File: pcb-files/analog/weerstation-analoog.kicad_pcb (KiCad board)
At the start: 2 copper layers, 99.1 x 99.1 mm, 60 parts, among them J1 i2c in out, J10 regensensor2 pins, J11 adc_alerts, J12 sound meter, J13 ADC 4 inputs, J2 power-in, J3 ads1115 (1), J4 ads1115 (2), J5 ads1115 (4), J6 ads1115 (3)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

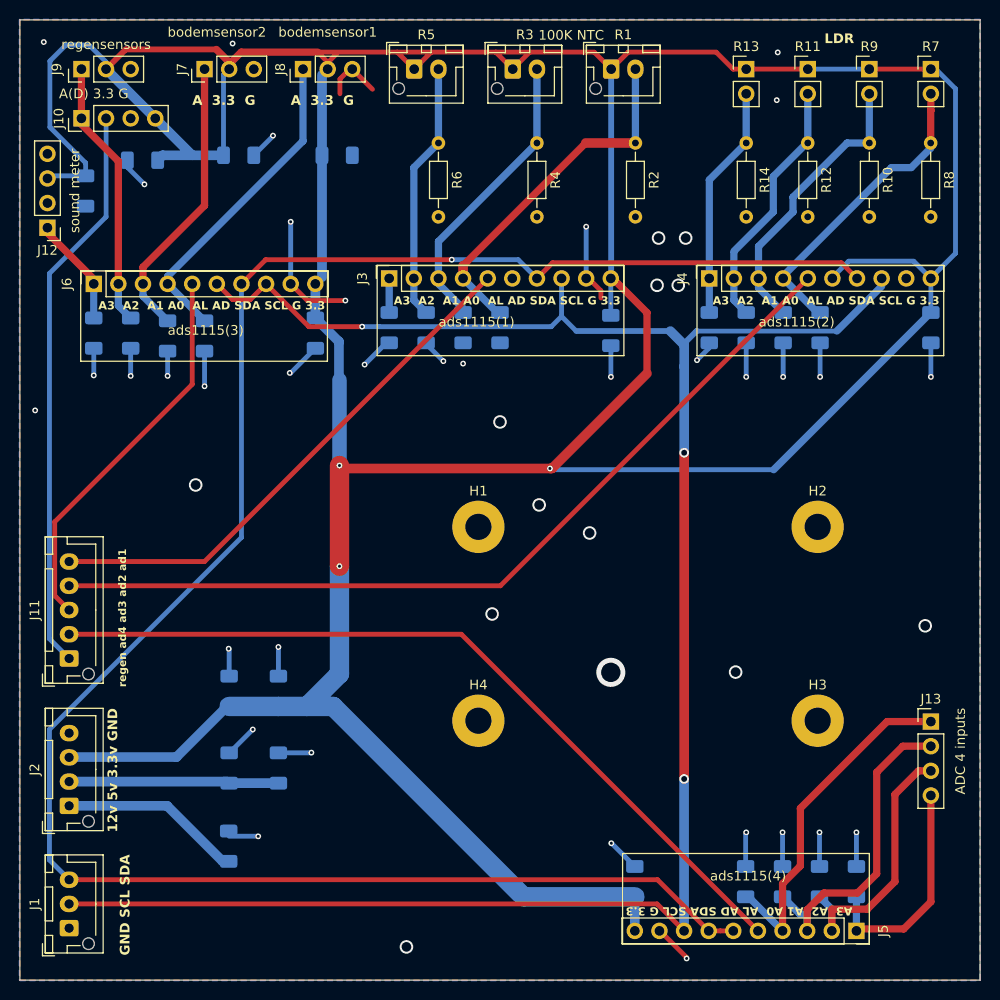
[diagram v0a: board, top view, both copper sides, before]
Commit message: pcbs as orderd. loads of grounding fixes
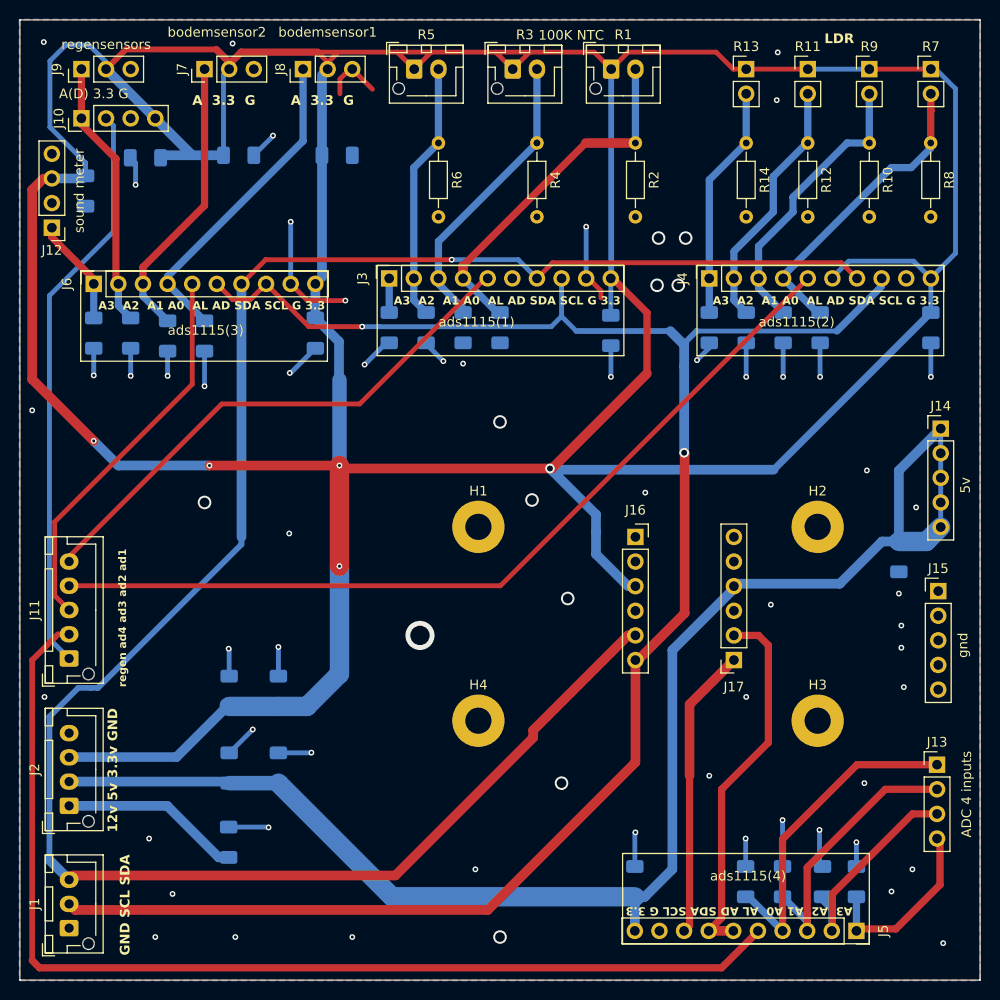
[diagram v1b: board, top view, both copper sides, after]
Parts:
- added C30: 10uf, Capacitor_SMD:C_1206_3216Metric_Pad1.33x1.80mm_HandSolder, B.Cu at (103.4, 68.1)
- added J14: 5v, Connector_PinHeader_2.54mm:PinHeader_1x05_P2.54mm_Vertical, F.Cu at (107.7, 54.9)
- added J15: gnd, Connector_PinHeader_2.54mm:PinHeader_1x05_P2.54mm_Vertical, F.Cu at (107.4, 71.6)
- added J16: levelshift lv, Connector_PinSocket_2.54mm:PinSocket_1x06_P2.54mm_Vertical, F.Cu at (76.2, 66.0)
- added J17: levelshift hv, Connector_PinSocket_2.54mm:PinSocket_1x06_P2.54mm_Vertical, F.Cu at (86.4, 78.7)
- moved J13 4.49 mm to (107.3, 89.5)
- moved J12 0.46 mm to (16.0, 34.1)
- moved C23 0.41 mm to (34.2, 97.5)
- moved C28 0.40 mm to (25.7, 26.9)
- moved C17 0.32 mm to (95.5, 101.6)
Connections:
- C12 pad 1: +3.3V -> +5V
- J5 pad 10: +3.3V -> +5V
- J5 pad 6: sda -> Net-(J17-Pin_2)
- J5 pad 7: sda -> Net-(J17-Pin_2)
- J5 pad 8: scl -> Net-(J17-Pin_1)
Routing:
- net +5V: track 21.7 -> 151.4 mm
- net Net-(J17-Pin_2): track 0.00 -> 38.5 mm
- net Net-(J17-Pin_1): track 0.00 -> 30.1 mm
- net ADC4 alert: track 83.7 -> 112.7 mm
- net +3.3V: track 458.6 -> 485.8 mm, vias 3 -> 5
- net scl: track 208.9 -> 193.3 mm, vias 3 -> 2
- net ADC-4 A2: track 27.7 -> 22.1 mm
- net ADC-4 A1: track 33.1 -> 27.8 mm
- net ADC-4 A3: track 23.4 -> 19.0 mm
- net GND: track 110.8 -> 108.5 mm, vias 48 -> 67
- net ADC-4 A0: track 35.8 -> 33.8 mm
- net regen-digitaal: track 59.0 -> 59.6 mm
